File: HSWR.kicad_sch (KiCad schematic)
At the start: 22 parts, among them J1 USB_B, J2 IO, J3 B+, J4 B-, J5 U, J6 V, J7 W, U14 Opamp_Quad

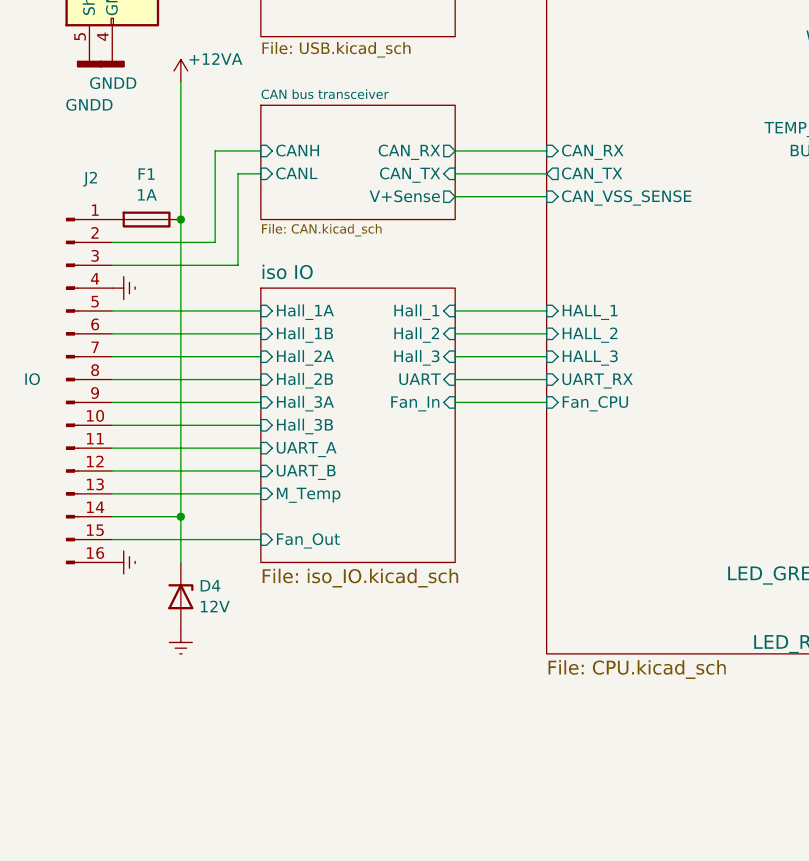
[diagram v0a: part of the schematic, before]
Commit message: - peeled back the filler planes around HV logic - improved insulation on HV logic
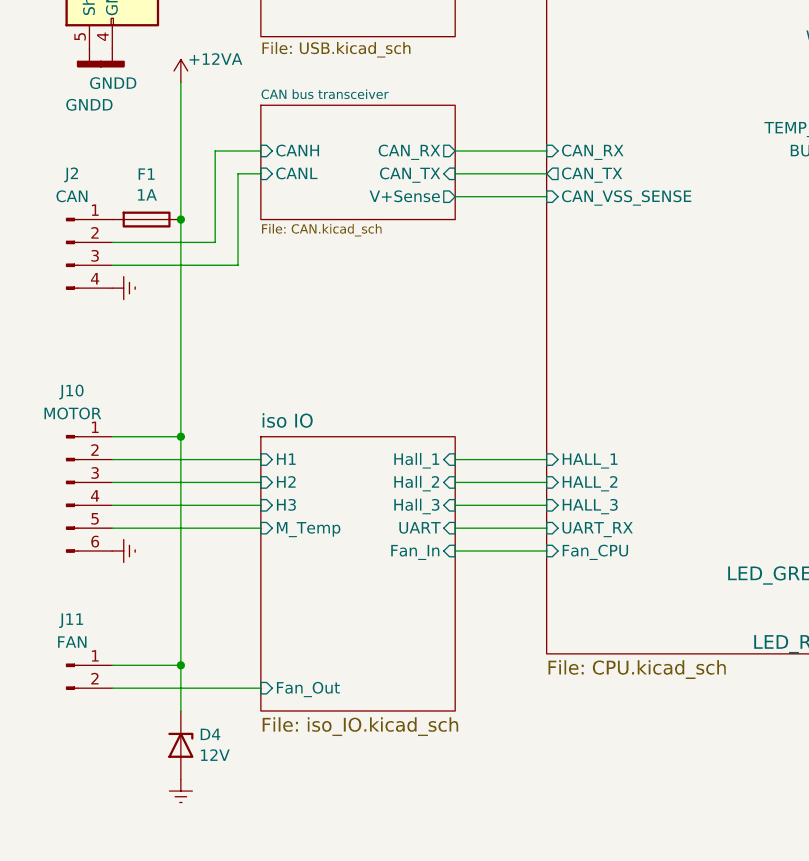
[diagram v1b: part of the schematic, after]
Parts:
- removed J2: IO, Connector_IDC:IDC-Header_2x08_P2.54mm_Vertical_Lock, symbol HSWR-rescue:Conn_01x16_Male-Connector
- added J10: MOTOR, Connector_Phoenix_MC:PhoenixContact_MCV_1,5_6-G-3.5_1x06_P3.50mm_Vertical, symbol Connector:Conn_01x06_Pin
- added J11: FAN, Connector_Phoenix_MC:PhoenixContact_MCV_1,5_2-G-3.5_1x02_P3.50mm_Vertical, symbol Connector:Conn_01x02_Pin
- added J2: CAN, Connector_Phoenix_MC:PhoenixContact_MCV_1,5_4-G-3.5_1x04_P3.50mm_Vertical, symbol Connector:Conn_01x04_Pin
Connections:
- net +12VA: now also J10.1 (Pin_1), J11.1 (Pin_1)
- net CAN bus transceiver/CANH: now also J2.2 (Pin_2)
- net CAN bus transceiver/CANL: now also J2.3 (Pin_3)
- net Earth: now also J10.6 (Pin_6), J2.4 (Pin_4)
- net iso IO/Fan_Out: now also J11.2 (Pin_2)
- net iso IO/M_Temp: now also J10.5 (Pin_5)
- net at F1.2: now also J2.1 (Pin_1)
- new net iso IO/H1: J10.2 (Pin_2)
- new net iso IO/H2: J10.3 (Pin_3)
- new net iso IO/H3: J10.4 (Pin_4)
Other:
- sheet iso IO ports: added H1, H2, H3; removed Hall_1A, Hall_1B, Hall_2A, Hall_2B, Hall_3A, Hall_3B, UART_A, UART_B
- moved on the sheet: D4

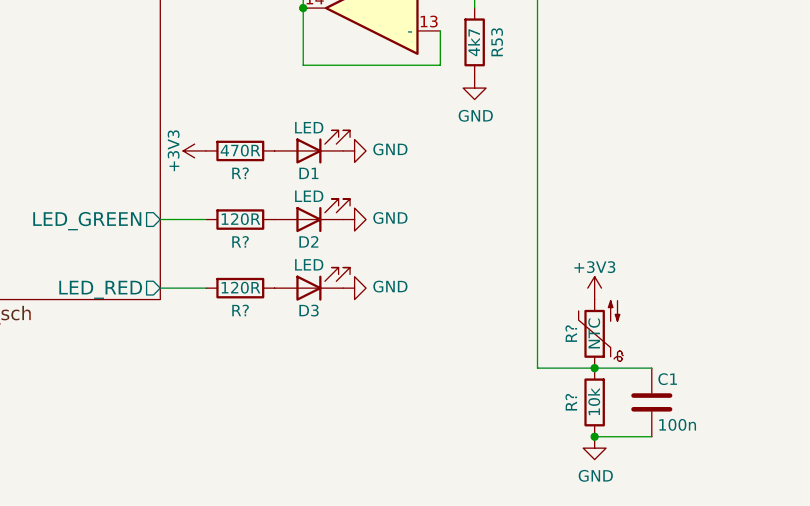
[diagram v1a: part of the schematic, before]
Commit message: - upgraded to KiCAD8
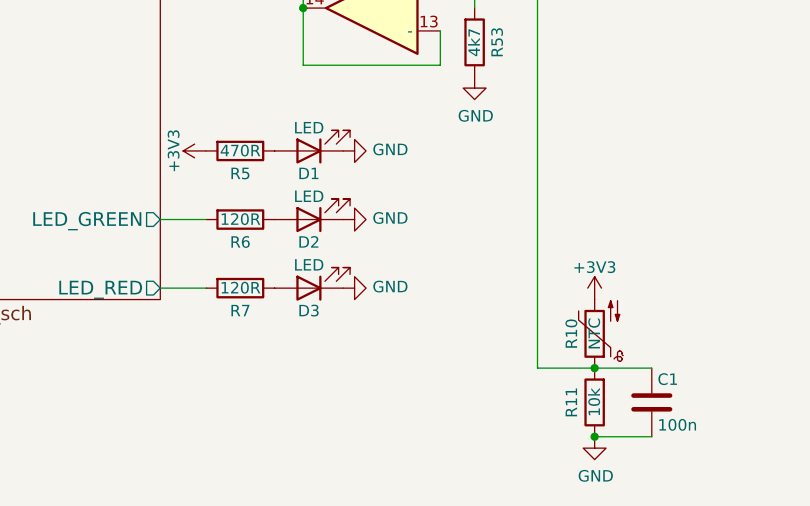
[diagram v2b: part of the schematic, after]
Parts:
- gave numbers to parts that had none: 5
